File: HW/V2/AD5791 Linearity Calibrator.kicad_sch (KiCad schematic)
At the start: 59 parts, among them J11 ISO OUT, J11 PWR, J2 VREFP, J3 VREFN, J5 VREFP, SW1 RST, U1 LM317, U11 ADuM1400xRW, U12 ADuM1201AR, U12 ISO7340C, U2 AD5791BRUZ, U2 LM337, U3 ADR1399, U3 LM317, U6 REFSCALE, U7 REFBUF, U8 Pico, U9 OUTBUF

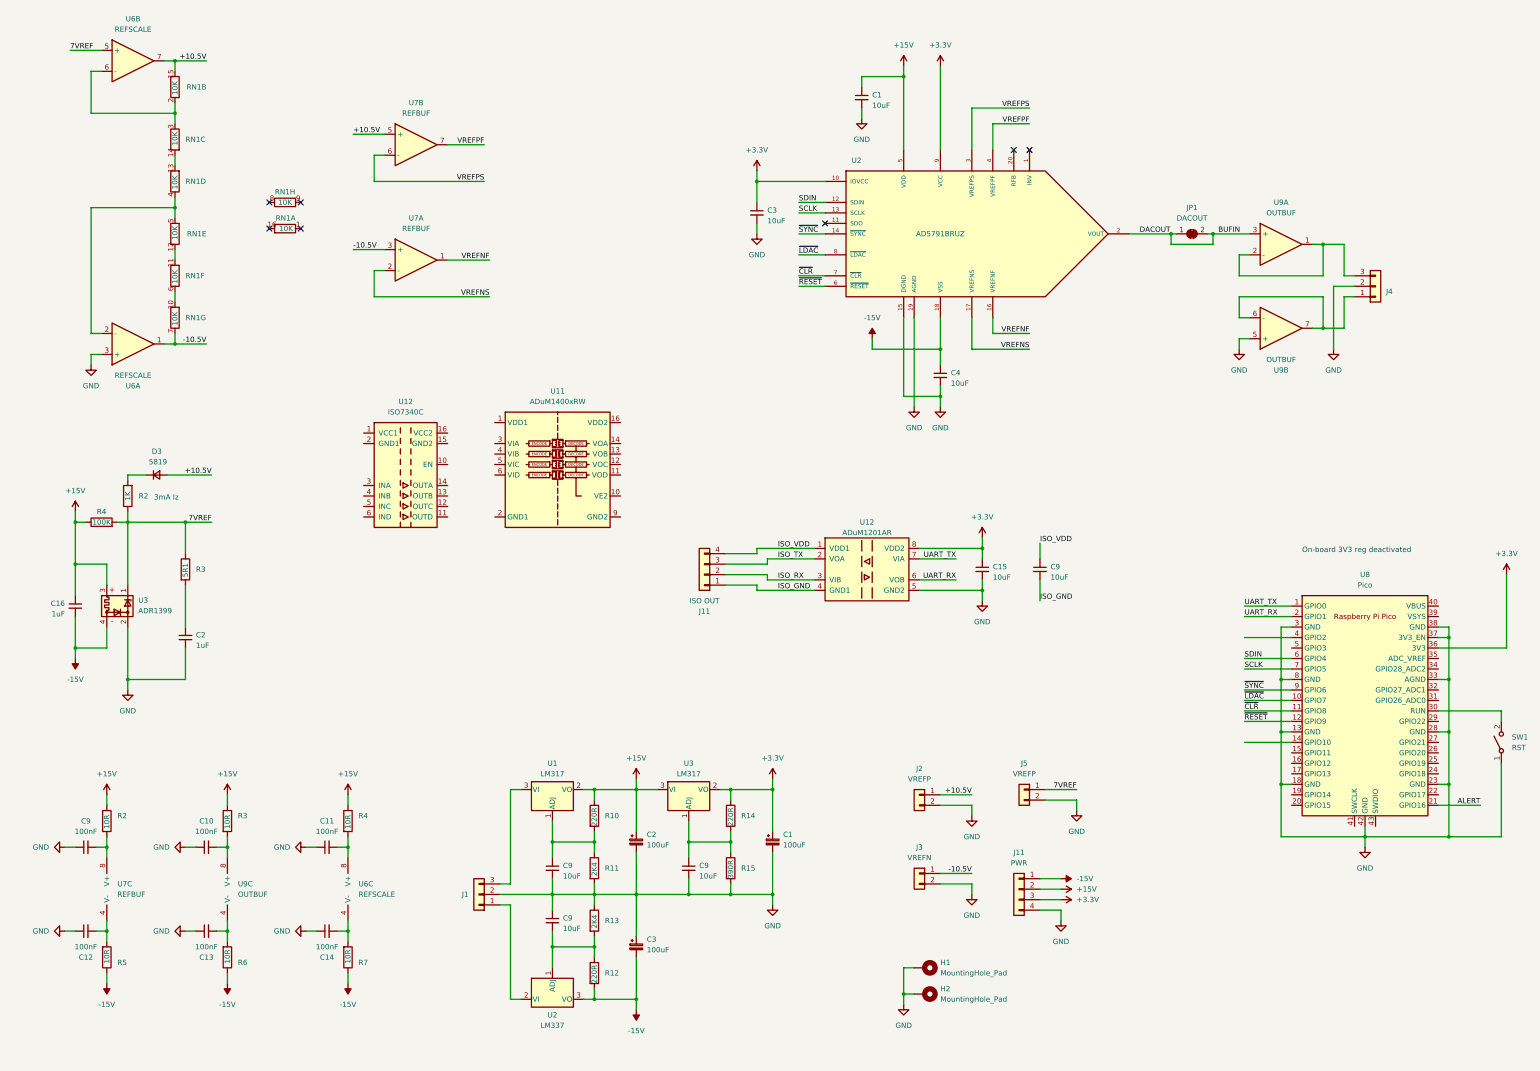
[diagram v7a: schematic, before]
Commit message: updated layout
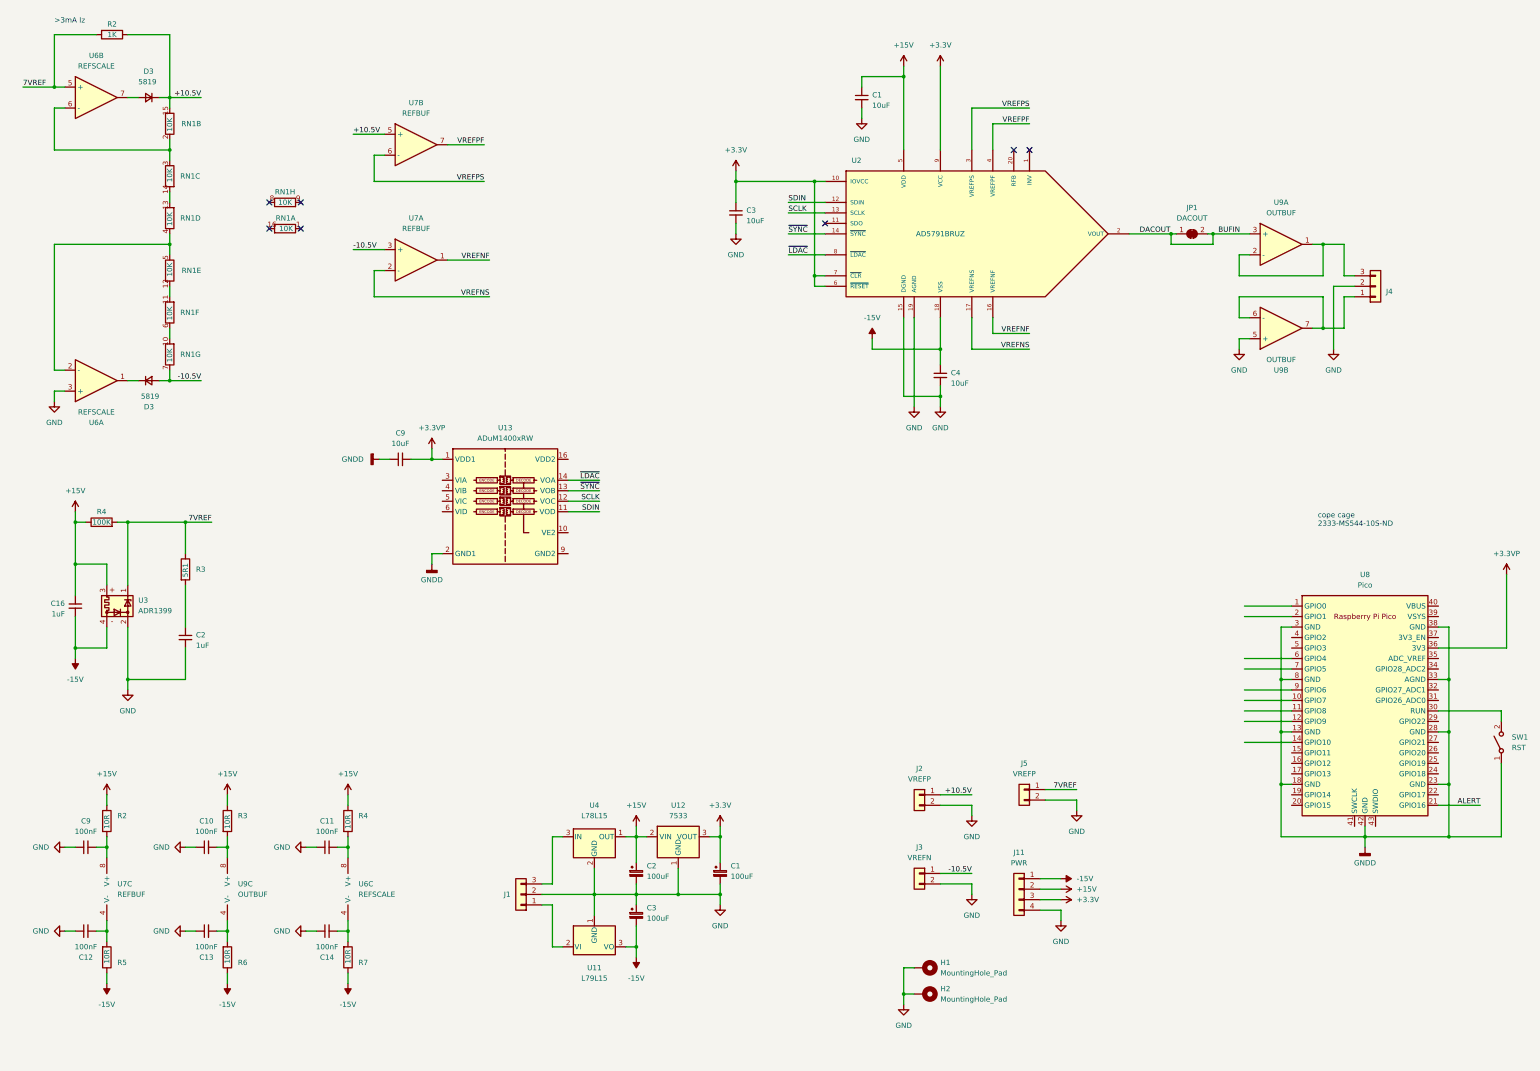
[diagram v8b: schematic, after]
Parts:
- removed C15, C9 (x4): 10uF, Resistor_SMD:R_0603_1608Metric, symbol Device:C_Small
- removed J11: ISO OUT, Connector_PinHeader_2.54mm:PinHeader_1x04_P2.54mm_Vertical, symbol Connector_Generic:Conn_01x04
- removed R10, R12, R14: 220R, Resistor_SMD:R_0603_1608Metric, symbol Device:R
- removed R11, R13: 2K4, Resistor_SMD:R_0603_1608Metric, symbol Device:R
- removed R15: 390R, Resistor_SMD:R_0603_1608Metric, symbol Device:R
- removed U1, U3: LM317, Package_TO_SOT_SMD:TO-252-2, symbol Regulator_Linear:LM317_TO-252
- removed U11: ADuM1400xRW, Package_SO:SOIC-16W_7.5x10.3mm_P1.27mm, symbol Isolator:ADuM1400xRW
- removed U12: ISO7340C, Package_SO:SOIC-16W_7.5x10.3mm_P1.27mm, symbol Isolator:ISO7340C
- removed U12: ADuM1201AR, Package_SO:SOIC-8_3.9x4.9mm_P1.27mm, symbol Isolator:ADuM1201AR
- removed U2: LM337, Package_TO_SOT_SMD:TO-252-2, symbol Regulator_Linear:LM337_TO252
- added C9: 10uF, Resistor_SMD:R_0603_1608Metric, symbol Device:C_Small
- added D3: 5819, Resistor_SMD:R_0603_1608Metric_Pad0.98x0.95mm_HandSolder, symbol Device:D_Small
- added U11: L79L15, Package_TO_SOT_SMD:SOT-89-3, symbol Regulator_Linear:L79L15_SOT89
- added U12: 7533, Package_TO_SOT_SMD:SOT-89-3, symbol Regulator_Linear:HT75xx-1-SOT89
- added U13: ADuM1400xRW, Package_SO:SOIC-16W_7.5x10.3mm_P1.27mm, symbol Isolator:ADuM1400xRW
- added U4: L78L15, Package_TO_SOT_SMD:SOT-89-3, symbol Regulator_Linear:L78L15_SOT89
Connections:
- net +10.5V: now also D3.1 (K), R2.1; no longer D3.2 (A), U6.7
- net +15V: now also U12.2 (VIN), U4.1 (OUT)
- net +3.3V: now also U2.6 (~{RESET}), U2.7 (~{CLR}), U12.3 (VOUT); no longer U8.36 (3V3)
- net -10.5V: now also D3.2 (A); no longer U6.1
- net -15V: now also U11.3 (VO)
- net 7VREF: now also R2.2; no longer R2.1
- net GND: now also U11.1 (GND), U12.1 (GND), U4.2 (GND); no longer SW1.1 (A), U8.13 (GND), U8.18 (GND), U8.23 (GND), U8.28 (GND), U8.3 (GND), U8.33 (AGND), U8.37 (3V3_EN), U8.38 (GND), U8.42 (GND), U8.8 (GND)
- net SCLK: now also U13.12 (VOC); no longer U8.7 (GPIO5)
- net SDIN: now also U13.11 (VOD); no longer U8.6 (GPIO4)
- net ~{LDAC}: now also U13.14 (VOA); no longer U8.10 (GPIO7)
- net ~{SYNC}: now also U13.13 (VOB); no longer U8.9 (GPIO6)
- net at J1.3 (Pin_3): now also U4.3 (IN)
- net at J1.1 (Pin_1): now also U11.2 (VI)
- net UART_RX: no longer names the net of U8.2 (GPIO1)
- net UART_TX: no longer names the net of U8.1 (GPIO0)
- net ~{CLR}: no longer names the net of U8.11 (GPIO8)
- net ~{CLR}: no longer U2.7 (~{CLR})
- net ~{RESET}: no longer names the net of U8.12 (GPIO9)
- net ~{RESET}: no longer U2.6 (~{RESET})
- new net: D3.2 (A), U6.7
- new net: D3.1 (K), U6.1
- new net: U13.15 (GND2), U13.9 (GND2)
- new net +3.3VP: C9.2, U13.1 (VDD1), U8.36 (3V3)
- new net GNDD: C9.1, SW1.1 (A), U13.2 (GND1), U13.8 (GND1), U8.13 (GND), U8.18 (GND), U8.23 (GND), U8.28 (GND), U8.3 (GND), U8.33 (AGND), U8.38 (GND), U8.42 (GND), U8.8 (GND)
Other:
- note added: ">3mA Iz"
- note added: "cope cage 2333-MS544-10S-ND"
- note removed: "3mA Iz"
- note removed: "On-board 3V3 reg deactivated"
- moved on the sheet: C1, C2, C3, D3, J1, R2, RN1B, RN1C, RN1D, RN1E, RN1F, RN1G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
